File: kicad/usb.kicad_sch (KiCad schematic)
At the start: 3 parts, among them J5 USB4145-03-0230-C

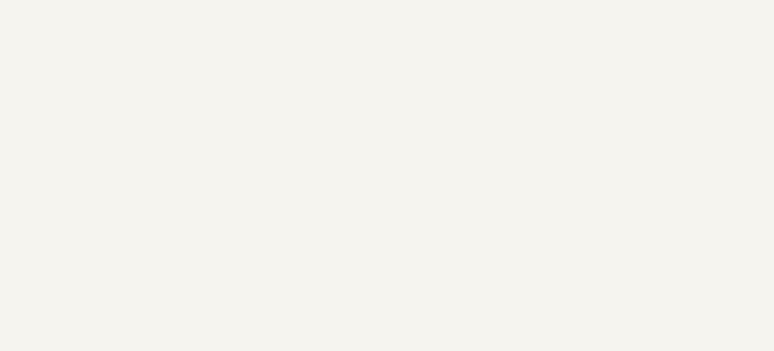
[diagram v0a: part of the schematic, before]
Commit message: Fixed power issue
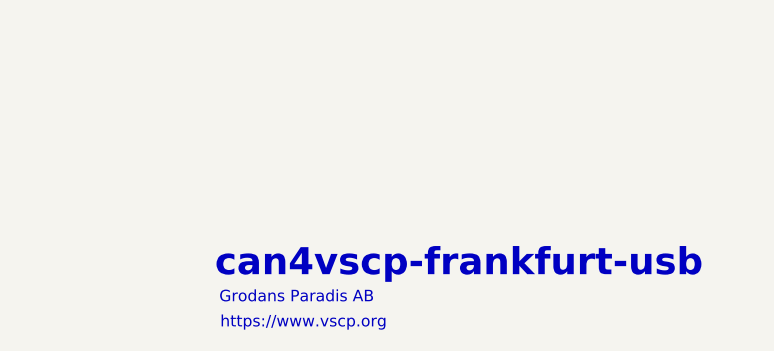
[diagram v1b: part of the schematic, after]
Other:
- note added: "Grodans Paradis AB"
- note added: "can4vscp-frankfurt-usb"
- note added: "https://www.vscp.org"
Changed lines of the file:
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@@
 	(generator_version "10.0")
 	(paper "A4")
+	(text "https://www.vscp.org"
+		(exclude_from_sim no)
+		(at 189.738 176.022 0)
+		(effects
+			(font
+				(size 1.27 1.27)
+			)
+		)
+	)
+	(text "Grodans Paradis AB"
+		(exclude_from_sim no)
+		(at 188.976 173.228 0)
+		(effects
+			(font
+				(size 1.27 1.27)
+			)
+		)
+	)
+	(text "can4vscp-frankfurt-usb"
+		(exclude_from_sim no)
+		(at 207.01 169.418 0)
+		(effects
+			(font
+				(size 3 3)
+				(thickness 0.6)
+				(bold yes)
+			)
+		)
+	)
 	(junction
 		(at 133.35 77.47)

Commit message: Reversion A schema and PCB
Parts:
- added IC6: ECMF02-2AMX6, Package_DFN_QFN:ST_UQFN-6L_1.5x1.7mm_P0.5mm, symbol Power_Protection:ECMF02-2AMX6
- J5: footprint CONN_USB4145-03-0230-C_GCT -> USB4145-03-0230-C:CONN_USB4145-03-0230-C_GCT
- R15, R16: footprint Resistors_SMD:R_0603 -> Resistor_SMD:R_0805_2012Metric
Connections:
- net GND: now also IC6.3 (GND), IC6.4 (NC)
- net USB_DN: now also IC6.5 (D-_out); no longer J5.A7 (DN1), J5.B6 (DP2)
- net USB_DP: now also IC6.6 (D+_out); no longer J5.A6 (DP1), J5.B7 (DN2)
- new net: IC6.1 (D+_in), J5.A6 (DP1), J5.B7 (DN2)
- new net: IC6.2 (D-_in), J5.A7 (DN1), J5.B6 (DP2)
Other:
- moved on the sheet: J5, R15, R16
